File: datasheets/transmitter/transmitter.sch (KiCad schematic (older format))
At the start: 6 parts, among them CON1 AVR-ISP-6, IC1 ATTINY85-P, Q1 Q_NPN_EBC

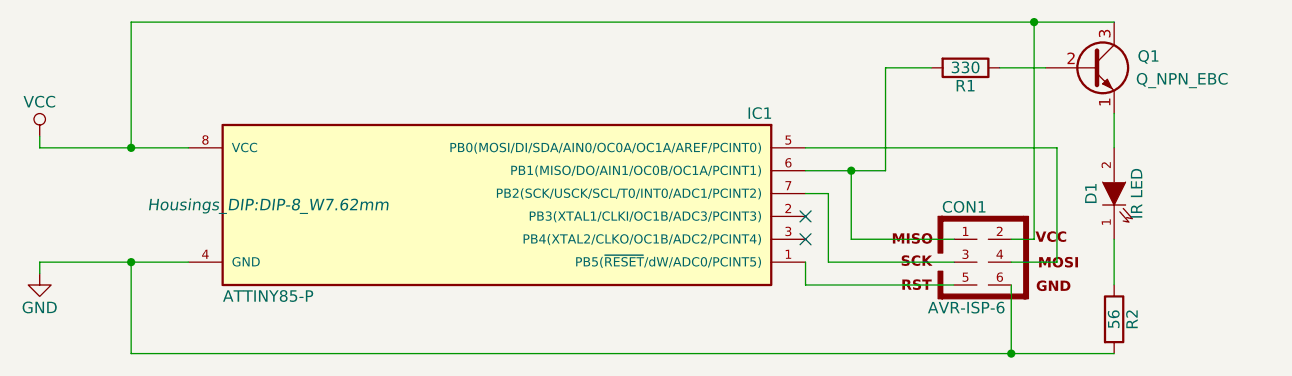
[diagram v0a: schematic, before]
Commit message: Reroute LED and transistor. Remove backup files from git.
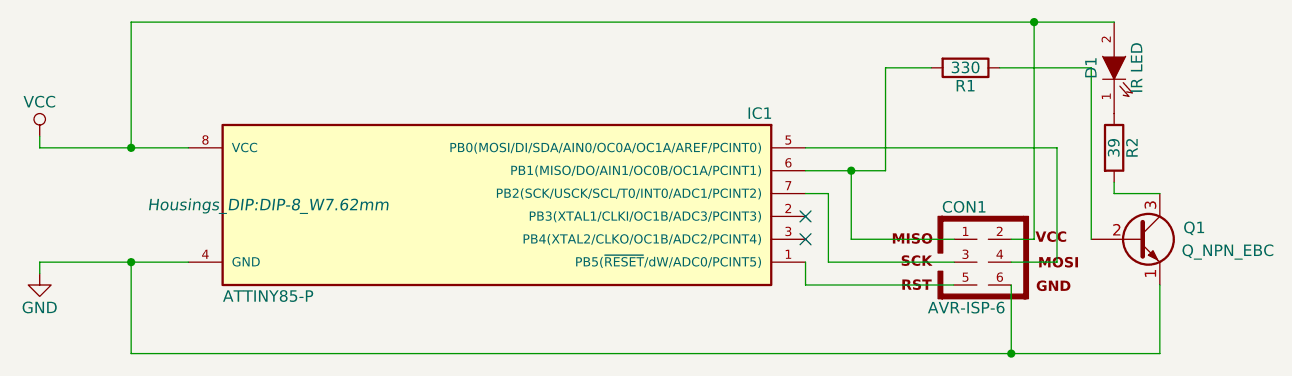
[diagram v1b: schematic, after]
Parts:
- R2: value 56 -> 39
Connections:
- net GND: now also Q1.1 (E); no longer R2.2
- net VCC: now also D1.2 (A); no longer Q1.3 (C)
- new net: Q1.3 (C), R2.2
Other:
- moved on the sheet: D1, Q1, R2
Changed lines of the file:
@@
 L LED D1
 U 1 1 56C0E26F
-P 8700 3700
-F 0 "D1" H 8700 3800 50  0000 C CNN
-F 1 "IR LED" H 8700 3600 50  0000 C CNN
-F 2 "Pin_Headers:Pin_Header_Straight_1x02" H 8700 3700 50  0001 C CNN
-F 3 "" H 8700 3700 50  0000 C CNN
-	1    8700 3700
+P 8700 3150
+F 0 "D1" H 8700 3250 50  0000 C CNN
+F 1 "IR LED" H 8700 3050 50  0000 C CNN
+F 2 "Pin_Headers:Pin_Header_Straight_1x02" H 8700 3150 50  0001 C CNN
+F 3 "" H 8700 3150 50  0000 C CNN
+	1    8700 3150
 	0    -1   -1   0
 $EndComp
@@
 L R R2
 U 1 1 56C0E2F4
-P 8700 4250
-F 0 "R2" V 8780 4250 50  0000 C CNN
-F 1 "56" V 8700 4250 50  0000 C CNN
-F 2 "Resistors_ThroughHole:Resistor_Horizontal_RM7mm" V 8630 4250 50  0001 C CNN
-F 3 "" H 8700 4250 50  0000 C CNN
-	1    8700 4250
+P 8700 3500
+F 0 "R2" V 8780 3500 50  0000 C CNN
+F 1 "39" V 8700 3500 50  0000 C CNN
+F 2 "Resistors_ThroughHole:Resistor_Horizontal_RM7mm" V 8630 3500 50  0001 C CNN
+F 3 "" H 8700 3500 50  0000 C CNN
+	1    8700 3500
 	1    0    0    -1
 $EndComp
@@
 L Q_NPN_EBC Q1
 U 1 1 56C0E336
-P 8600 3150
-F 0 "Q1" H 8900 3200 50  0000 R CNN
-F 1 "Q_NPN_EBC" H 9200 3100 50  0000 R CNN
-F 2 "TO_SOT_Packages_THT:TO-92_Inline_Narrow_Oval" H 8800 3250 50  0001 C CNN
-F 3 "" H 8600 3150 50  0000 C CNN
-	1    8600 3150
+P 8800 3900
+F 0 "Q1" H 9100 3950 50  0000 R CNN
+F 1 "Q_NPN_EBC" H 9400 3850 50  0000 R CNN
+F 2 "TO_SOT_Packages_THT:TO-92_Inline_Narrow_Oval" H 9000 4000 50  0001 C CNN
+F 3 "" H 8800 3900 50  0000 C CNN
+	1    8800 3900
 	1    0    0    -1
 $EndComp
@@
 Connection ~ 4400 3500
 Wire Wire Line
-	8200 3150 8400 3150
+	8200 3150 8600 3150
 Wire Wire Line
 	7900 3150 7700 3150
 Wire Wire Line
-	8700 3500 8700 3350
-Wire Wire Line
-	8700 3900 8700 4100
-Wire Wire Line
-	4400 4400 8700 4400
+	4400 4400 8900 4400
 Wire Wire Line
 	4400 4400 4400 4000
@@
 	8250 4100 8250 4400
 Connection ~ 8250 4400
-NoConn ~ 7350 3900
 Wire Wire Line
 	7700 3600 7700 3150
 Connection ~ 7550 3600
 $Comp
-L VCC #PWR?
+L VCC #PWR02
 U 1 1 56C27B48
 P 4000 3450
-F 0 "#PWR?" H 4000 3300 50  0001 C CNN
+F 0 "#PWR02" H 4000 3300 50  0001 C CNN
 F 1 "VCC" H 4000 3600 50  0000 C CNN
 F 2 "" H 4000 3450 50  0000 C CNN
@@
 	1    0    0    -1
 $EndComp
+Wire Wire Line
+	8600 3150 8600 3900
+Wire Wire Line
+	8900 3700 8700 3700
+Wire Wire Line
+	8700 3700 8700 3650
+Wire Wire Line
+	8900 4400 8900 4100
 NoConn ~ 7350 3800
+NoConn ~ 7350 3900
 $EndSCHEMATC
